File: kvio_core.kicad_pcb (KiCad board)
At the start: 6 copper layers, 60 x 41 mm, 175 parts, among them J1001 16-pin_FFC_(SFV16R), J1101 16-pin_FFC_(SFV16R), J1301 USB3_B_Micro, J401 16-pin_FFC_(SFV16R), J501 16-pin_FFC_(SFV16R), J601 16-pin_FFC_(SFV16R), J701 16-pin_FFC_(SFV16R), J801 16-pin_FFC_(SFV16R), J901 16-pin_FFC_(SFV16R), U1001 EMI8143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

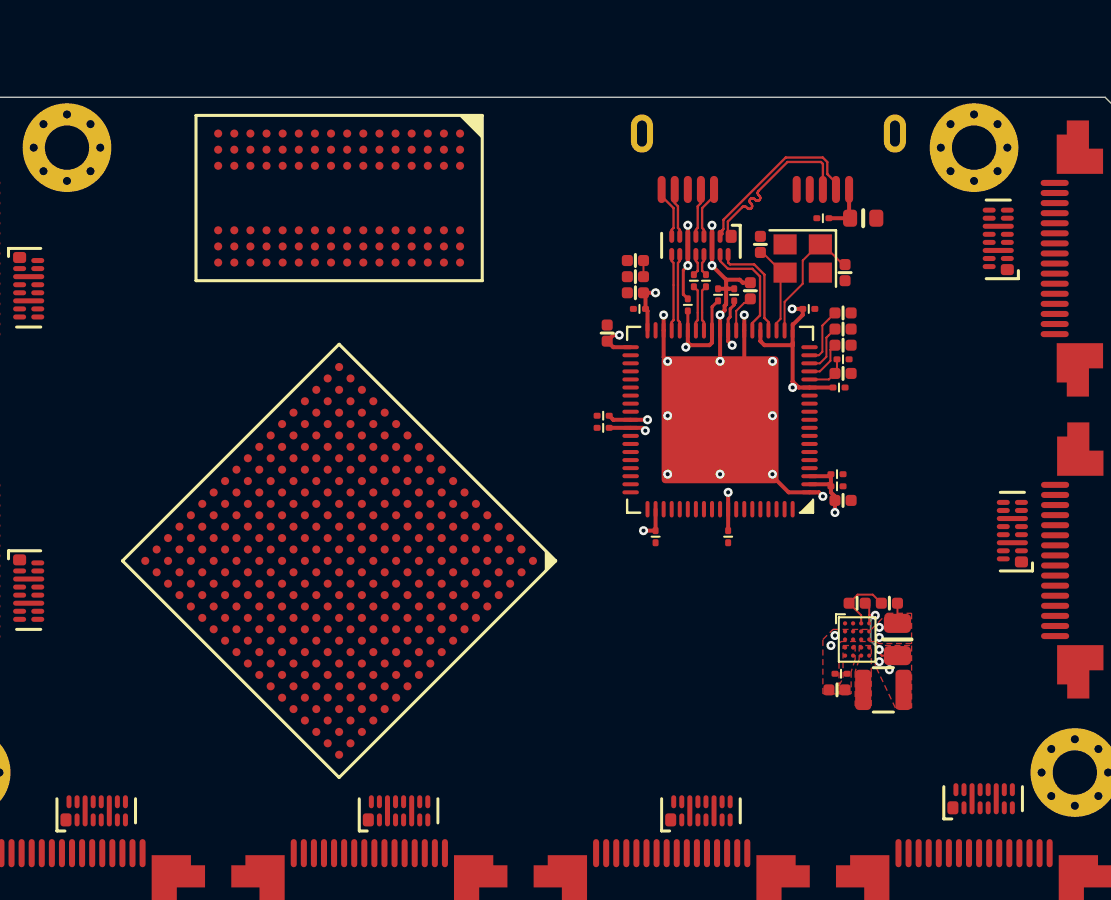
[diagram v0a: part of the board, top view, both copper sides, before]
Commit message: DDR3 routed, length matching left
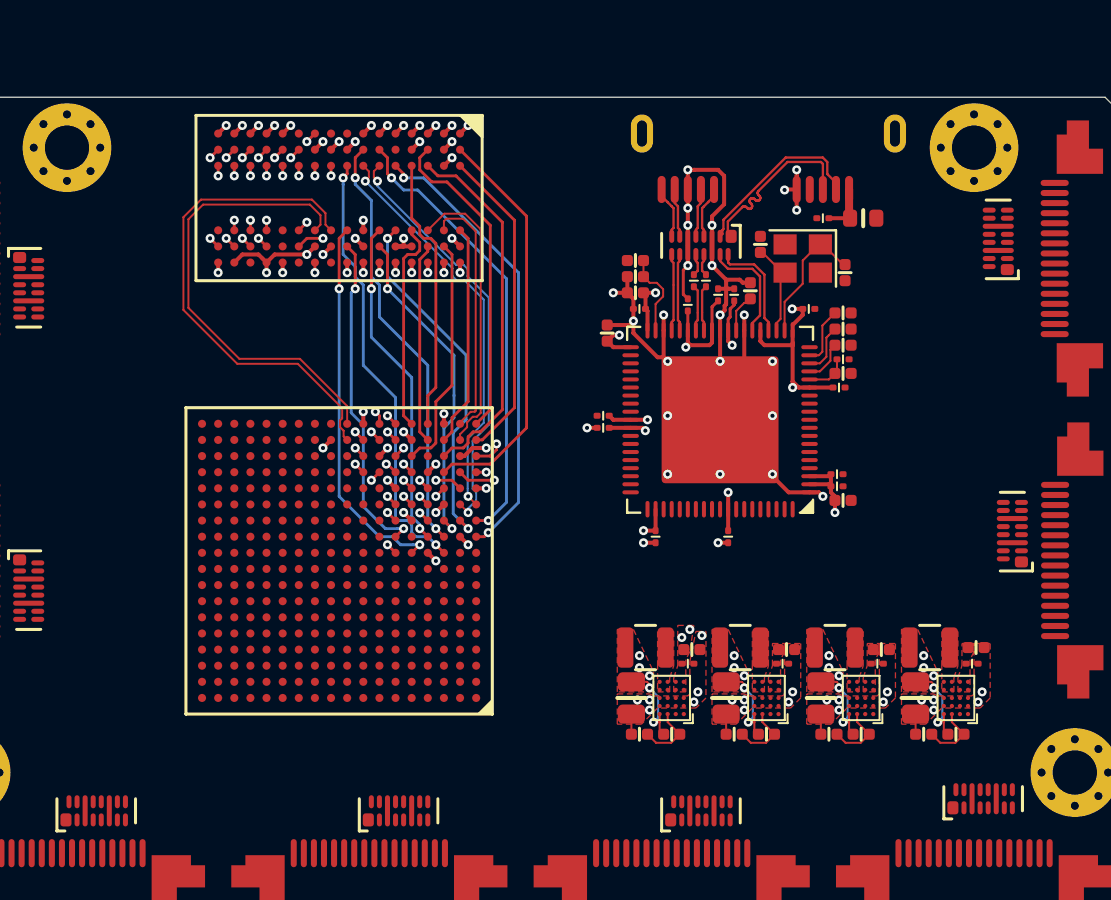
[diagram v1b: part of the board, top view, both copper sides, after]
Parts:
- added C274: 10u, passive:C_0402, F.Cu at (207.2, 116.4)
- added C275: 0.1u, passive:C_0201, F.Cu at (207.0, 117.1)
- added C276: 47u, passive:C_0805, F.Cu at (204.2, 118.8)
- added C277: 10u, passive:C_0402, F.Cu at (202.5, 116.4)
- added C278: 0.1u, passive:C_0201, F.Cu at (202.3, 117.1)
- added C279: 47u, passive:C_0805, F.Cu at (199.5, 118.8)
- added C280: 10u, passive:C_0402, F.Cu at (211.9, 116.4)
- added C281: 0.1u, passive:C_0201, F.Cu at (211.7, 117.1)
- added C282: 47u, passive:C_0805, F.Cu at (208.9, 118.8)
- added L202: 0.47uH, inductor:L_2025Metric, F.Cu at (204.9, 116.3)
- added L203: 0.47uH, inductor:L_2025Metric, F.Cu at (200.2, 116.3)
- added L204: 0.47uH, inductor:L_2025Metric, F.Cu at (209.6, 116.3)
- added R203: 0, passive:R_0402, F.Cu at (206.2, 120.6)
- added R204: 0, passive:R_0402, F.Cu at (204.6, 120.6)
- added R205: 0, passive:R_0402, F.Cu at (201.5, 120.6)
- added R206: 0, passive:R_0402, F.Cu at (199.9, 120.6)
- added R207: 0, passive:R_0402, F.Cu at (210.9, 120.6)
- added R208: 0, passive:R_0402, F.Cu at (209.3, 120.6)
- added U202: FAN53541, bga:WLCSP-20_1.96x1.56mm_Layout4x5_P0.4mm, F.Cu at (206.2, 118.8)
- added U203: FAN53541, bga:WLCSP-20_1.96x1.56mm_Layout4x5_P0.4mm, F.Cu at (201.5, 118.8)
- added U204: FAN53541, bga:WLCSP-20_1.96x1.56mm_Layout4x5_P0.4mm, F.Cu at (210.9, 118.8)
- moved R201 8.14 mm to (215.6, 120.6), turned to 0 degrees
- moved C271 7.21 mm to (216.6, 116.3), turned to 0 degrees
- moved R202 6.72 mm to (214.0, 120.6), turned to 0 degrees
- moved C272 6.52 mm to (216.4, 117.1), turned to 0 degrees
- moved U201 5.69 mm to (215.6, 118.8), turned to 180 degrees
- moved L201 3.11 mm to (214.3, 116.3), turned to 180 degrees
- moved C273 3.04 mm to (213.6, 118.8), turned to 270 degrees
- turned U101 to 180 degrees
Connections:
- net /Power/SW1 renamed /Power/SW33
- net /Power/VOUT renamed /Power/3V3
- U101 pad K3: /DDR Memory/DQ1 -> /DDR Memory/DQ4
- U101 pad K5: /DDR Memory/DQ5 -> /DDR Memory/DQ7
- U101 pad L1: /DDR Memory/LDM -> /DDR Memory/DQ0
- U101 pad L3: /DDR Memory/DQ2 -> /DDR Memory/DQ6
- U101 pad L4: /DDR Memory/DQ6 -> /DDR Memory/DQ1
- U101 pad L6: /DDR Memory/DQ7 -> /DDR Memory/DQ5
- U101 pad M1: /DDR Memory/DQ0 -> /DDR Memory/DQ2
- U101 pad M2: /DDR Memory/DQ4 -> /DDR Memory/LDM
- U101 pad M4: /DDR Memory/CAS_N -> /DDR Memory/WE_N
- U101 pad M6: /DDR Memory/A1 -> /DDR Memory/A13
- U101 pad N4: /DDR Memory/A2 -> /DDR Memory/A11
- U101 pad N5: /DDR Memory/CK_E -> /DDR Memory/A7
- U101 pad N6: /DDR Memory/A4 -> /DDR Memory/A9
- U101 pad P2: /DDR Memory/BA2 -> /DDR Memory/CS_N
- U101 pad P3: /DDR Memory/RAS_N -> /DDR Memory/BA2
- U101 pad P4: /DDR Memory/BA1 -> /DDR Memory/A10
- U101 pad P5: /DDR Memory/WE_N -> /DDR Memory/A5
- U101 pad R1: /DDR Memory/BA0 -> /DDR Memory/ODT
- U101 pad R2: /DDR Memory/A0 -> /DDR Memory/CAS_N
- U101 pad R5: /DDR Memory/ODT -> /DDR Memory/BA0
- U101 pad R6: /DDR Memory/A10 -> /DDR Memory/A1
- U101 pad R7: /DDR Memory/A5 -> /DDR Memory/A8
- U101 pad R8: /DDR Memory/A8 -> /DDR Memory/A6
- U101 pad T1: /DDR Memory/A3 -> /DDR Memory/RAS_N
- U101 pad T3: /DDR Memory/DQ14 -> /DDR Memory/DQ9
- U101 pad T5: /DDR Memory/DQ15 -> /DDR Memory/DQ14
- U101 pad T6: /DDR Memory/A12 -> /DDR Memory/CK_E
- U101 pad T8: /DDR Memory/A13 -> /DDR Memory/A4
- U101 pad U1: /DDR Memory/UDM -> /DDR Memory/DQ15
- U101 pad U3: /DDR Memory/DQ10 -> /DDR Memory/DQ12
- U101 pad U4: /DDR Memory/DQ9 -> /DDR Memory/DQ10
- U101 pad U6: /DDR Memory/A11 -> /DDR Memory/A0
- U101 pad U7: /DDR Memory/A7 -> /DDR Memory/A12
- U101 pad U8: /DDR Memory/CS_N -> /DDR Memory/BA1
- U101 pad V1: /DDR Memory/DQ8 -> /DDR Memory/DQ11
- U101 pad V4: /DDR Memory/DQ12 -> /DDR Memory/UDM
- U101 pad V5: /DDR Memory/DQ11 -> /DDR Memory/DQ8
- U101 pad V6: /DDR Memory/A6 -> /DDR Memory/A3
- U101 pad V7: /DDR Memory/A9 -> /DDR Memory/A2
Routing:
- net GND: track 28.2 -> 64.4 mm, vias 20 -> 72
- net /DDR Memory/RESET_N: track 0.00 -> 27.0 mm, vias 0 -> 2
- net /DDR Memory/A7: track 0.00 -> 26.1 mm, vias 0 -> 2
- net /DDR Memory/CK_P: track 0.00 -> 24.9 mm
- net /DDR Memory/A13: track 0.00 -> 24.9 mm, vias 0 -> 2
- net /DDR Memory/A5: track 0.00 -> 24.8 mm, vias 0 -> 2
- net /DDR Memory/A9: track 0.00 -> 23.5 mm, vias 0 -> 2
- net /DDR Memory/CK_N: track 0.00 -> 23.1 mm
- net /DDR Memory/CAS_N: track 0.00 -> 23.1 mm, vias 0 -> 2
- net /DDR Memory/WE_N: track 0.00 -> 23.0 mm, vias 0 -> 2
- net /DDR Memory/ODT: track 0.00 -> 22.7 mm, vias 0 -> 2
- net /DDR Memory/DQ0: track 0.00 -> 22.6 mm, vias 0 -> 2
- net /DDR Memory/DQ2: track 0.00 -> 22.4 mm, vias 0 -> 2
- net /DDR Memory/CS_N: track 0.00 -> 22.1 mm, vias 0 -> 2
- net /DDR Memory/DQ4: track 0.00 -> 22.0 mm, vias 0 -> 2
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- added copper zone on F.Cu, net /Power/1V0
- added copper zone on F.Cu, net /Power/1V35
- added copper zone on F.Cu, net /Power/1V8
- added copper zone on F.Cu, net /Power/SW10
- added copper zone on F.Cu, net /Power/SW13
- added copper zone on F.Cu, net /Power/SW18
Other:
- net class 100 ohm diff inner: trace_width 0.2 -> 0.095
- net class 100 ohm diff outer: trace_width 0.0889 -> 0.098
- net class 40 ohm inner: trace_width 0.222 -> 0.221
- net class 40 ohm outer: trace_width 0.222 -> 0.227
- net class 50 ohm inner: trace_width 0.538 -> 0.134
- net class 50 ohm outer: trace_width 0.147 -> 0.142
- net class 80 ohm diff inner added: clearance 0.1, trace_width 0.123, via_dia 0.45, via_drill 0.2
- net class 80 ohm diff outer added: clearance 0.1, trace_width 0.145, via_dia 0.45, via_drill 0.2
- net class 90 ohm diff inner added: clearance 0.1, trace_width 0.111, via_dia 0.45, via_drill 0.2
- net class 90 ohm diff outer: clearance 0.1016 -> 0.1; trace_width 0.1173 -> 0.103

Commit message: Before length matching
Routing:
- net /DDR Memory/DQ1: track 16.5 -> 22.1 mm
- net /DDR Memory/DQ7: track 18.9 -> 21.1 mm
- net /DDR Memory/DQ5: track 16.4 -> 17.8 mm
- net /DDR Memory/LDM: track 17.7 -> 19.0 mm
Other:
- net class DDR3_CONTROL_LM1.0 added: clearance 0.1, trace_width 0.134, via_dia 0.45, via_drill 0.2
- net class DDR3_DBUS0_LM1.0 added: clearance 0.1, trace_width 0.142, via_dia 0.45, via_drill 0.2
- net class DDR3_DBUS1_LM1.0 added: clearance 0.1, trace_width 0.142, via_dia 0.45, via_drill 0.2

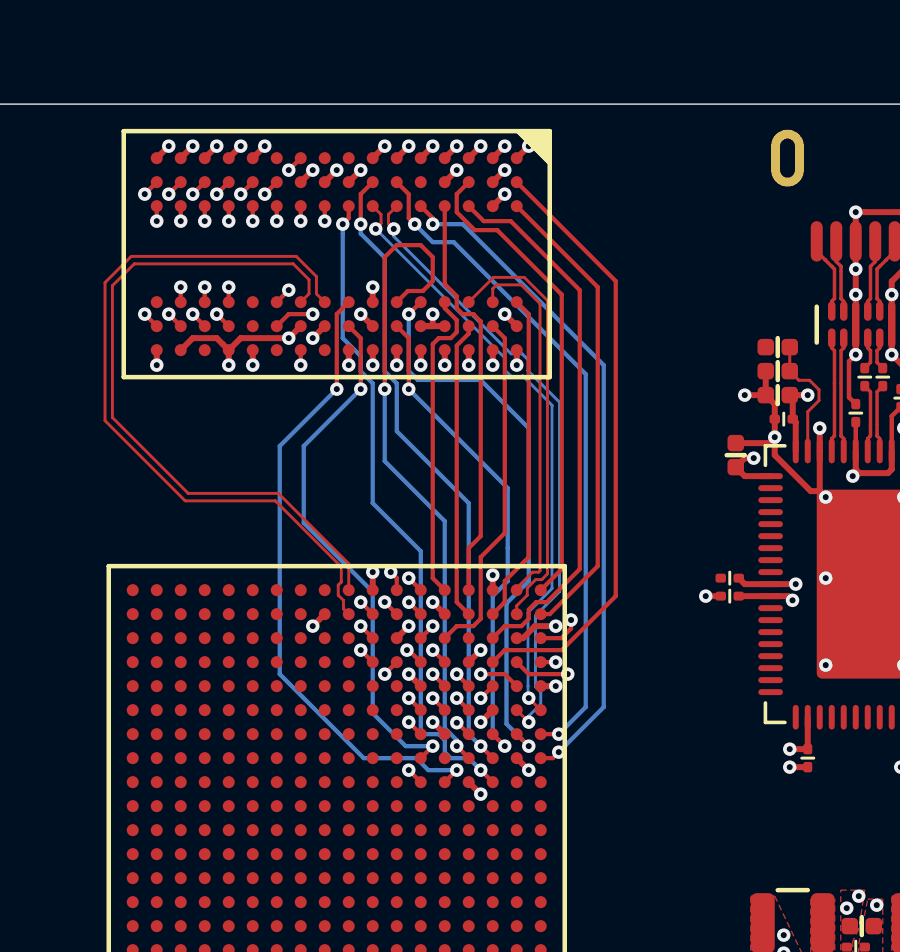
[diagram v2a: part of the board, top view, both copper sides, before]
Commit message: Data groups length matched
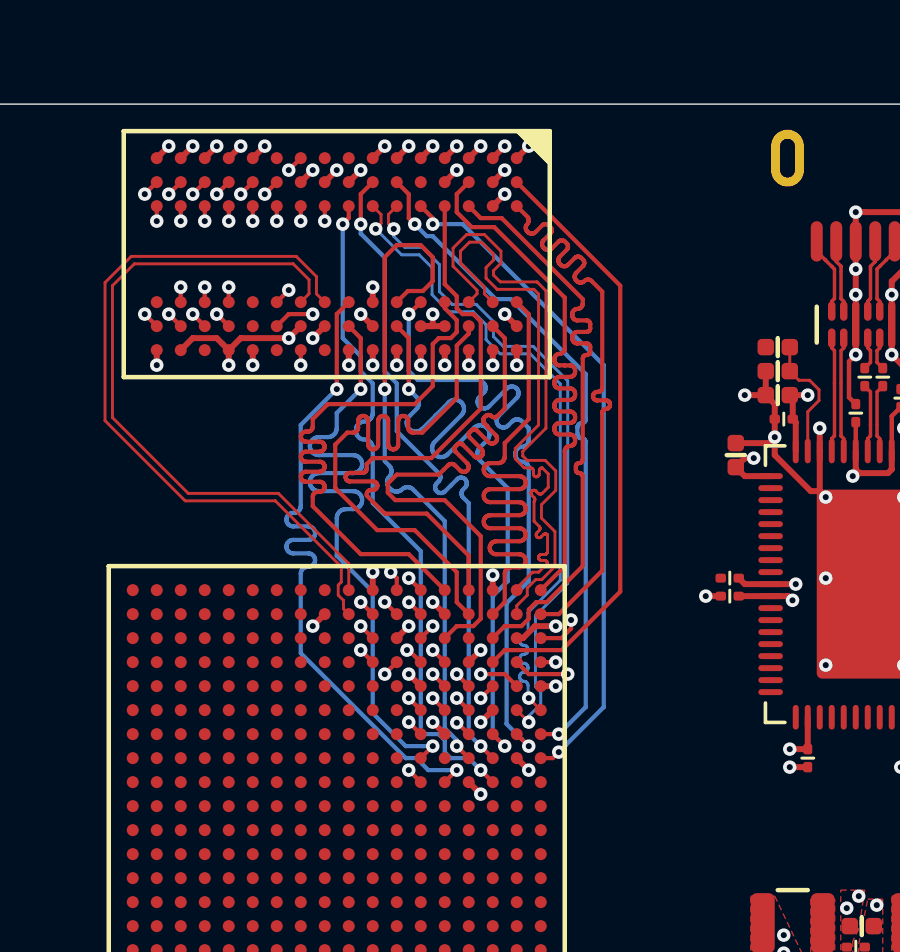
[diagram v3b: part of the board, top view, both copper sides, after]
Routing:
- net /DDR Memory/DQ10: track 9.93 -> 20.2 mm
- net /DDR Memory/DQ8: track 10.5 -> 20.2 mm
- net /DDR Memory/DQ12: track 11.1 -> 20.2 mm
- net /DDR Memory/DQ14: track 11.7 -> 20.2 mm
- net /DDR Memory/UDQS_N: track 12.3 -> 20.1 mm
- net /DDR Memory/UDM: track 13.7 -> 20.2 mm
- net /DDR Memory/DQ3: track 16.5 -> 22.6 mm
- net /DDR Memory/UDQS_P: track 14.3 -> 20.1 mm
- net /DDR Memory/DQ5: track 17.8 -> 22.6 mm
- net /DDR Memory/DQ15: track 15.7 -> 20.2 mm
- net /DDR Memory/DQ11: track 15.9 -> 20.2 mm
- net /DDR Memory/LDM: track 19.0 -> 22.6 mm
- net /DDR Memory/LDQS_N: track 20.2 -> 22.5 mm
- net /DDR Memory/DQ9: track 18.2 -> 20.2 mm
- net /DDR Memory/DQ7: track 21.1 -> 22.6 mm
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
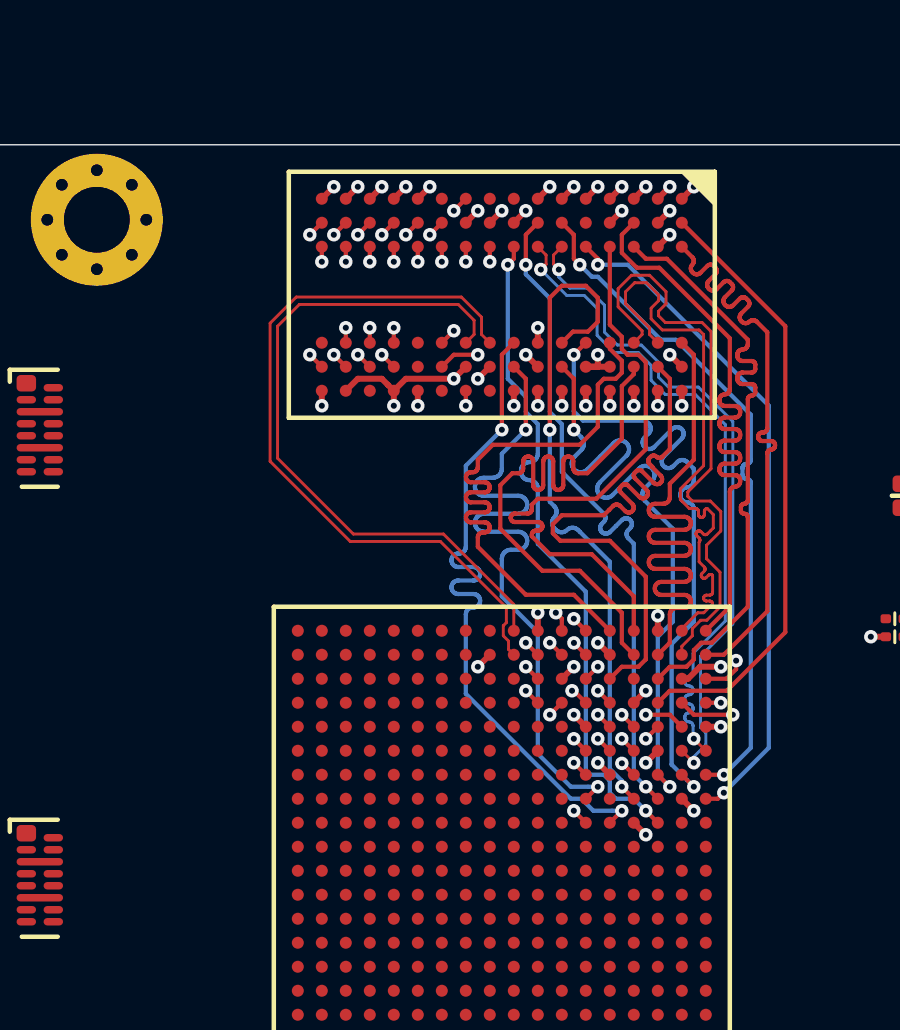
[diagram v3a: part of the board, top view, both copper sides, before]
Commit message: Length matching done (except CK, needs final layers)
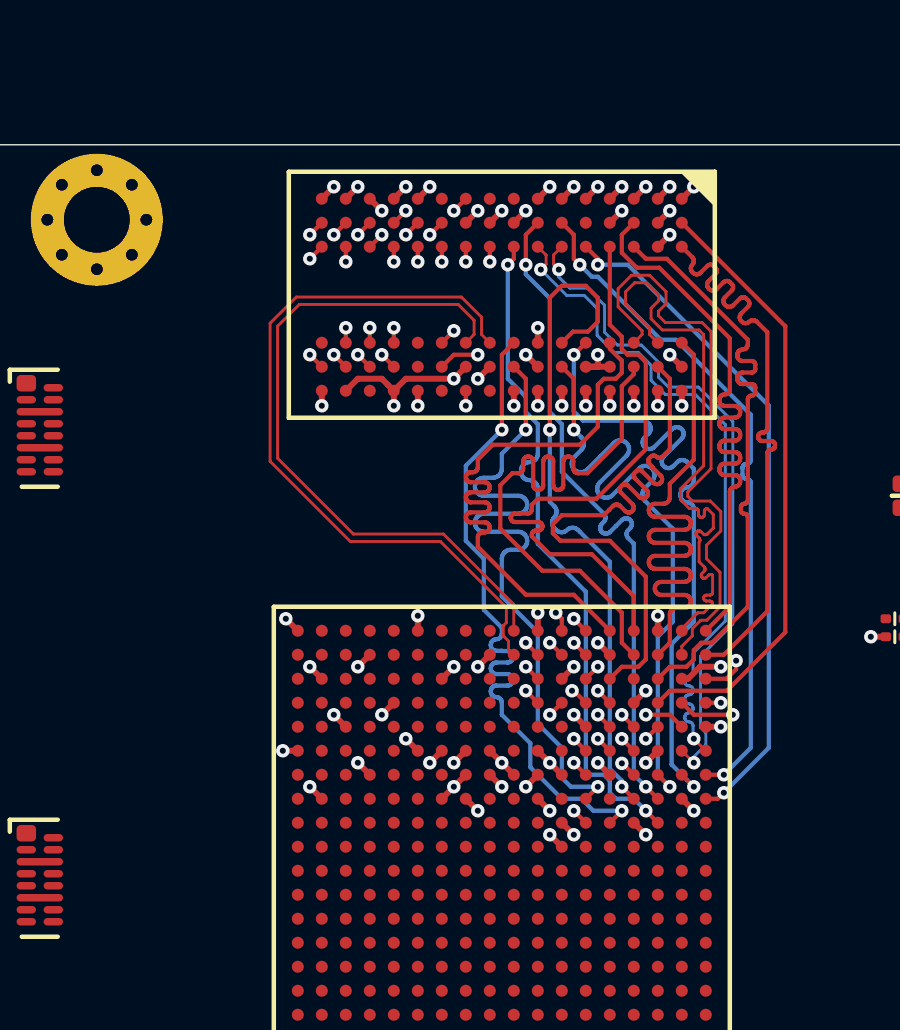
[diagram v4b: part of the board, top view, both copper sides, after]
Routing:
- net /DDR Memory/CK_E: track 12.5 -> 26.2 mm
- net /DDR Memory/BA1: track 12.7 -> 26.2 mm
- net /DDR Memory/A12: track 13.7 -> 26.1 mm
- net /DDR Memory/A4: track 14.0 -> 26.2 mm
- net /DDR Memory/A2: track 15.5 -> 26.2 mm
- net /DDR Memory/A6: track 15.8 -> 26.2 mm
- net /DDR Memory/A1: track 16.3 -> 26.2 mm
- net /DDR Memory/A3: track 16.6 -> 26.3 mm
- net /DDR Memory/A0: track 16.6 -> 26.1 mm
- net /DDR Memory/A10: track 17.2 -> 26.2 mm
- net /DDR Memory/A8: track 17.5 -> 26.2 mm
- net GND: track 64.4 -> 72.2 mm, vias 72 -> 83
- net /DDR Memory/A11: track 20.0 -> 26.1 mm
- net /DDR Memory/BA0: track 20.2 -> 26.2 mm
- net /DDR Memory/BA2: track 20.6 -> 26.2 mm
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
